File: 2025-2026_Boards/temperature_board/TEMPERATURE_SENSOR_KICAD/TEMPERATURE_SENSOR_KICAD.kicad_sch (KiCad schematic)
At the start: 39 parts, among them U1 STM32G431CBT6, U2 TMP235A4DBZR, U3 AMS1117-3.3, U4 TPS54240DGQ

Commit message: added voltage regulators. wired lcd pinout. added fan pinouts. added 2nd buck converter.
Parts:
- added C24, C25: 22u, Capacitor_SMD:C_0805_2012Metric, symbol Device:C
- added Cboot, Css, Css1: 33n, symbol Device:C
- added Cboot1, Cinx, Cinx1: 100n, symbol Device:C
- added Cin, Cin1: 10u, symbol Device:C
- added Cout, Cout1: 47u, symbol Device:C
- added D10, D11, D12, D13, D14, D15, D16, D17, D18, D19, D20, D21, D22, D23, D24, D25, D26, D27, D28, D29, D3, D30, D31, D32, D33, D34, D4, D5, D6, D7, D8, D9: 1N4148WT, Diode_SMD:D_SOD-523, symbol Diode:1N4148WT
- added D35: LED, Capacitor_SMD:C_0201_0603Metric, symbol Device:LED
- added J1: LCD Connector Pinout, symbol Connector_Generic_MountingPin:Conn_01x12_MountingPin
- added J2, J3: Conn_01x03_Pin, symbol Connector:Conn_01x03_Pin
- added L2: 10u, symbol Device:L
- added L3: 22u, symbol Device:L
- added R9: 1k5, Resistor_SMD:R_0402_1005Metric, symbol Device:R
- added RR1: 130, Resistor_SMD:R_0402_1005Metric, symbol Device:R
- added RR2: 100, Resistor_SMD:R_0402_1005Metric, symbol Device:R
- added Rfbb, Rfbb1: 10k, symbol Device:R
- added Rfbt: 52.3k, symbol Device:R
- added Rfbt1: 140k, symbol Device:R
- added U5, U6: TPS62932DRLR, SOT8_DRL_TEX, symbol 2025-10-19_16-52-39:TPS62932DRLR
- added U8: AMS1117, Package_TO_SOT_SMD:SOT-223-3_TabPin2, symbol Regulator_Linear:AMS1117
- L1: value L -> 10u
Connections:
- net +28V: now also C24.2, C25.1, C25.2, Cin.2, Cin1.2, Cinx.2, Cinx1.2, Cout.2, Cout1.2, Css.2, Css1.2, D35.2 (A), J2.2 (Pin_2), J3.2 (Pin_2), R9.2, RR1.1, RR2.2, Rfbb.2, Rfbb1.2, U5.4 (GND), U6.4 (GND), U8.2 (VO)
- net PWR_LED_K: now also D35.1 (K), R9.1
- net VBUS renamed +5V
- net +5V: now also C24.1, J3.1 (Pin_1), U8.3 (VI)
- new net: D12.1 (K), D25.1 (K), D28.1 (K), D4.1 (K), J1.7 (Pin_7)
- new net: D11.2 (A), D12.2 (A), D13.2 (A), D14.2 (A), D15.2 (A), D16.2 (A), D17.2 (A), D18.2 (A), J1.9 (Pin_9)
- new net: Cboot1.1, U6.6 (BST)
- new net: Cboot1.2, L3.1, U6.5 (SW)
- new net: D13.1 (K), D24.1 (K), D29.1 (K), D5.1 (K), J1.4 (Pin_4)
- new net: D27.2 (A), D28.2 (A), D29.2 (A), D30.2 (A), D31.2 (A), D32.2 (A), D33.2 (A), D34.2 (A), J1.6 (Pin_6)
- new net: D15.1 (K), D22.1 (K), D31.1 (K), D7.1 (K), J1.1 (Pin_1)
- new net: D19.2 (A), D20.2 (A), D21.2 (A), D22.2 (A), D23.2 (A), D24.2 (A), D25.2 (A), D26.2 (A), J1.8 (Pin_8)
- new net: D14.1 (K), D23.1 (K), D30.1 (K), D6.1 (K), J1.2 (Pin_2)
- new net: D10.1 (K), D18.1 (K), D19.1 (K), D34.1 (K), J1.3 (Pin_3)
- new net: D10.2 (A), D3.2 (A), D4.2 (A), D5.2 (A), D6.2 (A), D7.2 (A), D8.2 (A), D9.2 (A), J1.12 (Pin_12)
- new net: D11.1 (K), D26.1 (K), D27.1 (K), D3.1 (K), J1.11 (Pin_11)
- new net: Rfbb1.1, Rfbt1.2, U6.8 (FB)
- new net: D16.1 (K), D21.1 (K), D32.1 (K), D8.1 (K), J1.10 (Pin_10)
- new net: D17.1 (K), D20.1 (K), D33.1 (K), D9.1 (K), J1.5 (Pin_5)
- new net: Rfbb.1, Rfbt.2, U5.8 (FB)
- new net: Css1.1, U6.7 (SS)
- new net: RR1.2, RR2.1, U8.1 (ADJ)
- new net: Cboot.1, U5.6 (BST)
- new net: Cboot.2, L2.1, U5.5 (SW)
- new net: Css.1, U5.7 (SS)
- new net +12V: J2.1 (Pin_1)
- new net 12V: Cout1.1, L3.2, Rfbt1.1
- new net 28V: Cin.1, Cin1.1, Cinx.1, Cinx1.1, U5.3 (VIN), U6.3 (VIN)
- new net 5V: Cout.1, L2.2, Rfbt.1
- no-connect marks 0 -> 4
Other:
- note added: "BUCK CONVERTER (28V TO 12V, 2A)"
- note added: "BUCK CONVERTER (28V TO 5V, 2A)"
- note added: "CAMERA FAN PINOUT"
- note added: "ECORE FAN PINOUT"
- note added: "FAN PINOUTS"
- note added: "ON/OFF SIGNAL"
- note added: "STM32 / TMP23X VOLTAGE REGULATOR, 5V TO 3.3V"
- note removed: "FAN SYSTEMS AND POWER SUPPLY"
- note removed: "LCD AND POWER SUPPLY"
- note removed: "STM32 / TMP23X VOLTAGE REGULATOR"
- moved on the sheet: C1, C10, C11, C12, C13, C14, C15, C16, C17, C18, C19, C2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

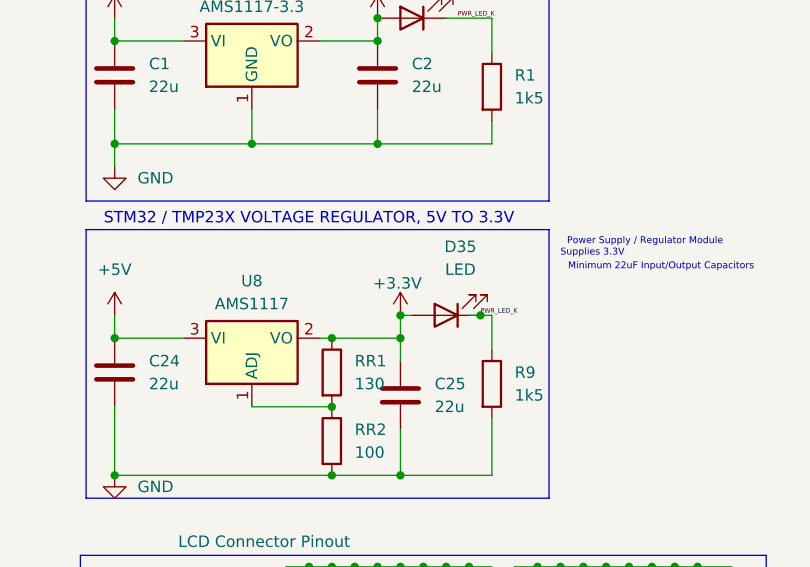
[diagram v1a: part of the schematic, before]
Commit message: 3.3->2.2V
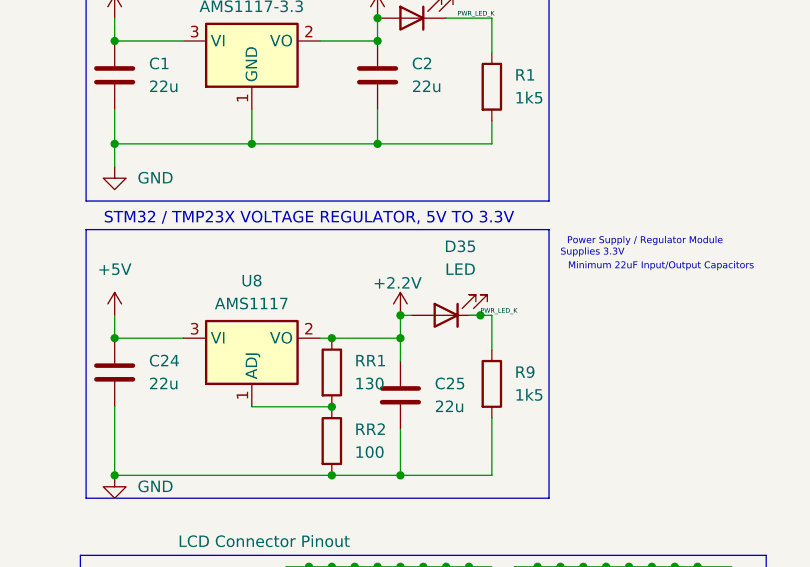
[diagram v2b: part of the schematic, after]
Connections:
- net +28V: no longer C25.1, D35.2 (A), RR1.1, U8.2 (VO)
- new net +2.2V: C25.1, D35.2 (A), RR1.1, U8.2 (VO)
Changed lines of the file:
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@@
 			)
 		)
-		(property "Value" "+3.3V"
+		(property "Value" "+2.2V"
 			(at 45.212 106.934 0)
 			(effects

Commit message: connected LCD pins to GPIO. Replicated ECORE fans and connectd to GPIO
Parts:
- removed J2: Conn_01x03_Pin, symbol Connector:Conn_01x03_Pin
- added J10, J11, J4, J5, J6, J7, J8, J9: Conn_01x03_Pin, symbol Connector:Conn_01x03_Pin
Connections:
- net +12V: now also J10.1 (Pin_1), J11.1 (Pin_1), J4.1 (Pin_1), J5.1 (Pin_1), J6.1 (Pin_1), J7.1 (Pin_1), J8.1 (Pin_1), J9.1 (Pin_1)
- net +28V: now also C14.1, J10.2 (Pin_2), J11.2 (Pin_2), J4.2 (Pin_2), J5.2 (Pin_2), J6.2 (Pin_2), J7.2 (Pin_2), J8.2 (Pin_2), J9.2 (Pin_2); no longer C14.2
- net at D12.1 (K), D25.1 (K), D28.1 (K)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: now also U1.17 (PB1)
- net at D11.2 (A), D12.2 (A), D13.2 (A)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: now also U1.5 (PF0)
- net at D13.1 (K), D24.1 (K), D29.1 (K)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: now also U1.41 (PB4)
- net at D27.2 (A), D28.2 (A), D29.2 (A)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: now also U1.28 (PB14)
- net at D15.1 (K), D22.1 (K), D31.1 (K)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: now also U1.44 (PB7)
- net at D19.2 (A), D20.2 (A), D21.2 (A)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: now also U1.29 (PB15)
- net at D14.1 (K), D23.1 (K), D30.1 (K)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: now also U1.43 (PB6)
- net at U1.11 (PA3): now also C14.2, R2.1
- net at U1.3 (PC14): now also D11.1 (K), D26.1 (K), D27.1 (K), D3.1 (K), J1.11 (Pin_11)
- net at U1.31 (PA9): now also J10.3 (Pin_3), J11.3 (Pin_3), J4.3 (Pin_3), J5.3 (Pin_3), J6.3 (Pin_3), J7.3 (Pin_3), J8.3 (Pin_3), J9.3 (Pin_3)
- net at U1.4 (PC15): now also D16.1 (K), D21.1 (K), D32.1 (K), D8.1 (K), J1.10 (Pin_10)
- net at U1.40 (PB3): now also D17.1 (K), D20.1 (K), D33.1 (K), D9.1 (K), J1.5 (Pin_5)
- net at U1.42 (PB5): now also D10.1 (K), D18.1 (K), D19.1 (K), D34.1 (K), J1.3 (Pin_3)
- net at U1.7 (PG10): now also D10.2 (A), D3.2 (A), D4.2 (A), D5.2 (A), D6.2 (A), D7.2 (A), D8.2 (A), D9.2 (A), J1.12 (Pin_12)
- now unconnected: U1.30 (PA8)
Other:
- note added: "STM32 / TMP23X VOLTAGE REGULATOR, 5V TO 2.2V"
- note removed: "FAN PINOUTS"
- moved on the sheet: C1, C10, C11, C12, C13, C14, C2, C24, C25, C3, C4, C5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

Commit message: Fixed fan pins in schematic. Started PCB layout. Wiring LDOs and buck converters.
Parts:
- removed C15, C16: 2.2u, Capacitor_SMD:C_0201_0603Metric, symbol Device:C
- removed C17: 0.01u, Capacitor_SMD:C_0201_0603Metric, symbol Device:C
- removed C18: C, symbol Device:C
- removed C19, C20, C23: 47u, symbol Device:C
- removed C21: 3300pf, Capacitor_SMD:C_0201_0603Metric, symbol Device:C
- removed C22: 15pf, Capacitor_SMD:C_0201_0603Metric, symbol Device:C
- removed D2: B360, Diode_SMD:D_SMC, symbol Diode:B360
- removed J10, J11, J3, J4, J5, J6, J7, J8, J9: Conn_01x03_Pin, symbol Connector:Conn_01x03_Pin
- removed L1: 10u, symbol Device:L
- removed R3: 124k, symbol Device:R
- removed R4: 30.1k, symbol Device:R
- removed R5: 412k, symbol Device:R
- removed R6: 37.4k, symbol Device:R
- removed R7: 10.0k, symbol Device:R
- removed R8: 45.3k, symbol Device:R
- removed U4: TPS54240DGQ, Package_SO:HVSSOP-10-1EP_3x3mm_P0.5mm_EP1.57x1.88mm_ThermalVias, symbol Converter_DCDC:TPS54240DGQ
- C14, Cboot1: footprint (none) -> Capacitor_SMD:C_0402_1005Metric
- Cboot2: renamed from Cboot; footprint (none) -> Capacitor_SMD:C_0201_0603Metric
- Cin1, Cout1: footprint (none) -> Capacitor_SMD:C_1210_3225Metric
- Cin2: renamed from Cin; footprint (none) -> Capacitor_SMD:C_1210_3225Metric
- Cinx1: footprint (none) -> Capacitor_SMD:C_0603_1608Metric
- Cinx2: renamed from Cinx; footprint (none) -> Capacitor_SMD:C_0603_1608Metric
- Cout2: renamed from Cout; footprint (none) -> Capacitor_SMD:C_1210_3225Metric
- Css1: footprint (none) -> Capacitor_SMD:C_01005_0402Metric
- Css2: renamed from Css; footprint (none) -> Capacitor_SMD:C_01005_0402Metric
- J1: footprint (none) -> Connector_FFC-FPC:Amphenol_F32Q-1A7x1-11012_1x12-1MP_P0.5mm_Horizontal
- L2: footprint (none) -> Inductor_SMD:L_Bourns_SRR1208_12.7x12.7mm
- L3: footprint (none) -> Inductor_THT:L_Radial_D13.5mm_P7.00mm_Fastron_09HCP
- R2: value 10R -> 10k; footprint (none) -> Resistor_SMD:R_0402_1005Metric
- Rfbb1: footprint (none) -> Resistor_SMD:R_0402_1005Metric
- Rfbb2: renamed from Rfbb; footprint (none) -> Resistor_SMD:R_0402_1005Metric
- Rfbt1: footprint (none) -> Resistor_SMD:R_0201_0603Metric
- Rfbt2: renamed from Rfbt; footprint (none) -> Resistor_SMD:R_0603_1608Metric
- U2: footprint DBZ0003A-IPC_A -> AdditionalFootprintLibrary:DBZ0003A-IPC_A
- U5, U6: footprint SOT8_DRL_TEX -> AdditionalFootprintLibrary:SOT8_DRL_TEX-M
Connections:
- net PWR_LED_K: no longer D35.1 (K), R9.1
- net +28V renamed GND
- net GND: no longer C11.1, C12.1, C13.1, C2.1, C3.1, C4.1, C5.1, C6.1, C7.1, D1.2 (A), U1.1 (VBAT), U1.24 (VDD), U1.36 (VDD), U1.48 (VDD), U2.1 (VDD), U3.2 (VO)
- new net: D35.1 (K), R9.1
- new net +3.3V: C11.1, C12.1, C13.1, C2.1, C3.1, C4.1, C5.1, C6.1, C7.1, D1.2 (A), U1.1 (VBAT), U1.24 (VDD), U1.36 (VDD), U1.48 (VDD), U2.1 (VDD), U3.2 (VO)
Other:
- added sheet Fan_Pins (FAN_PINS.kicad_sch)
- note added: "Supplies 2.2V"
- note removed: "BUCK CONVERTER (Early Draft, subject to change)"
- note removed: "CAMERA FAN PINOUT"
- note removed: "ECORE FAN PINOUT"
- note removed: "ON/OFF SIGNAL"
- moved on the sheet: C1, C2, C24, C25, D1, D35, R1, R9, RR1, RR2, U3, U8

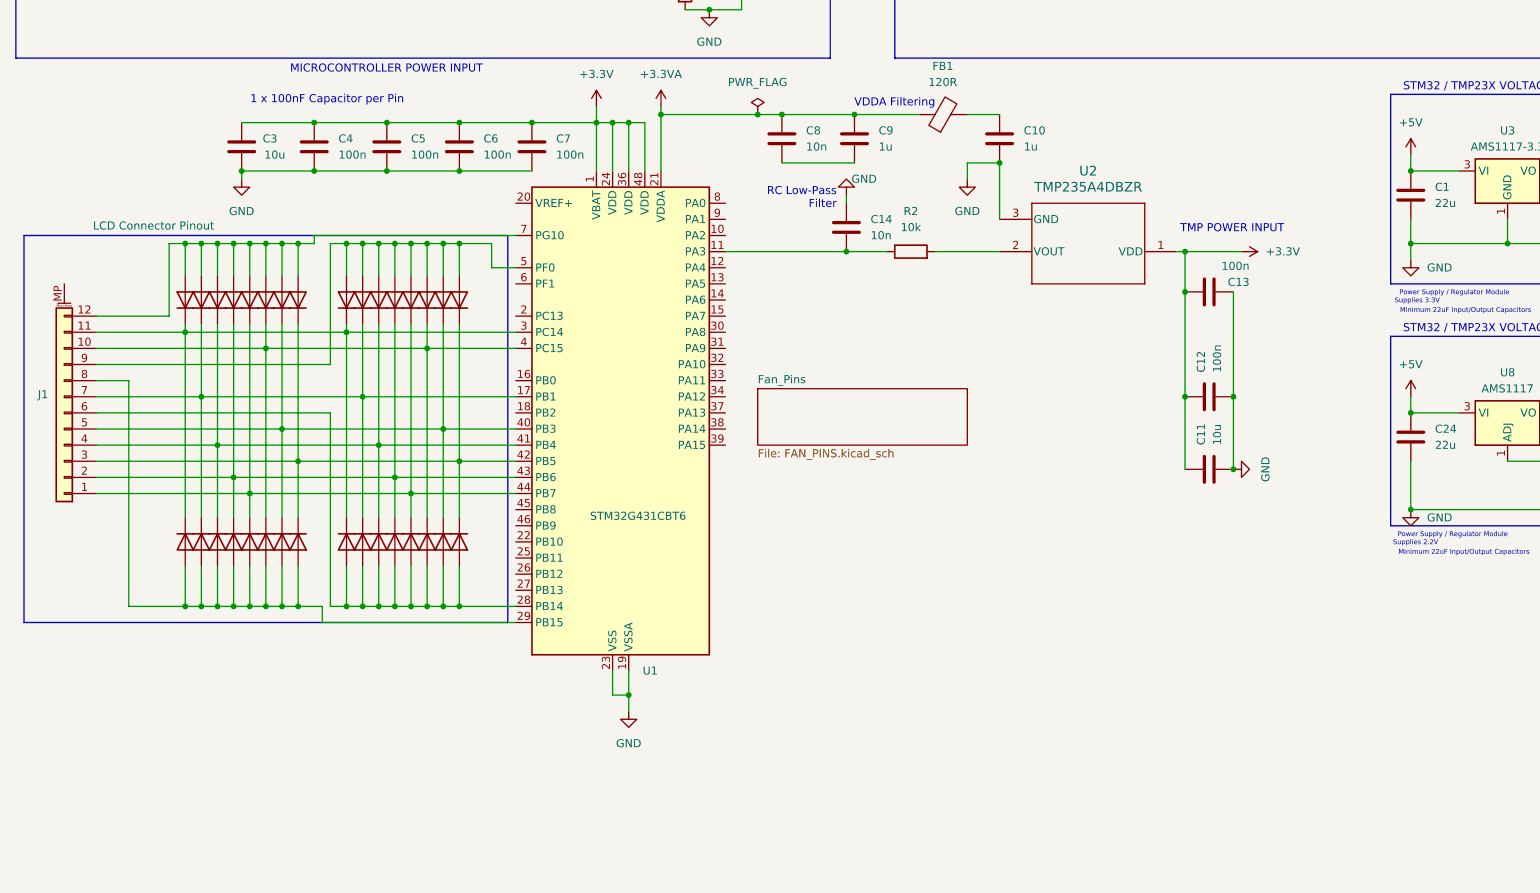
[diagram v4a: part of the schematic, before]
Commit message: Almost finished wiring. Just need to adjust widths and check configuration before finalizing design
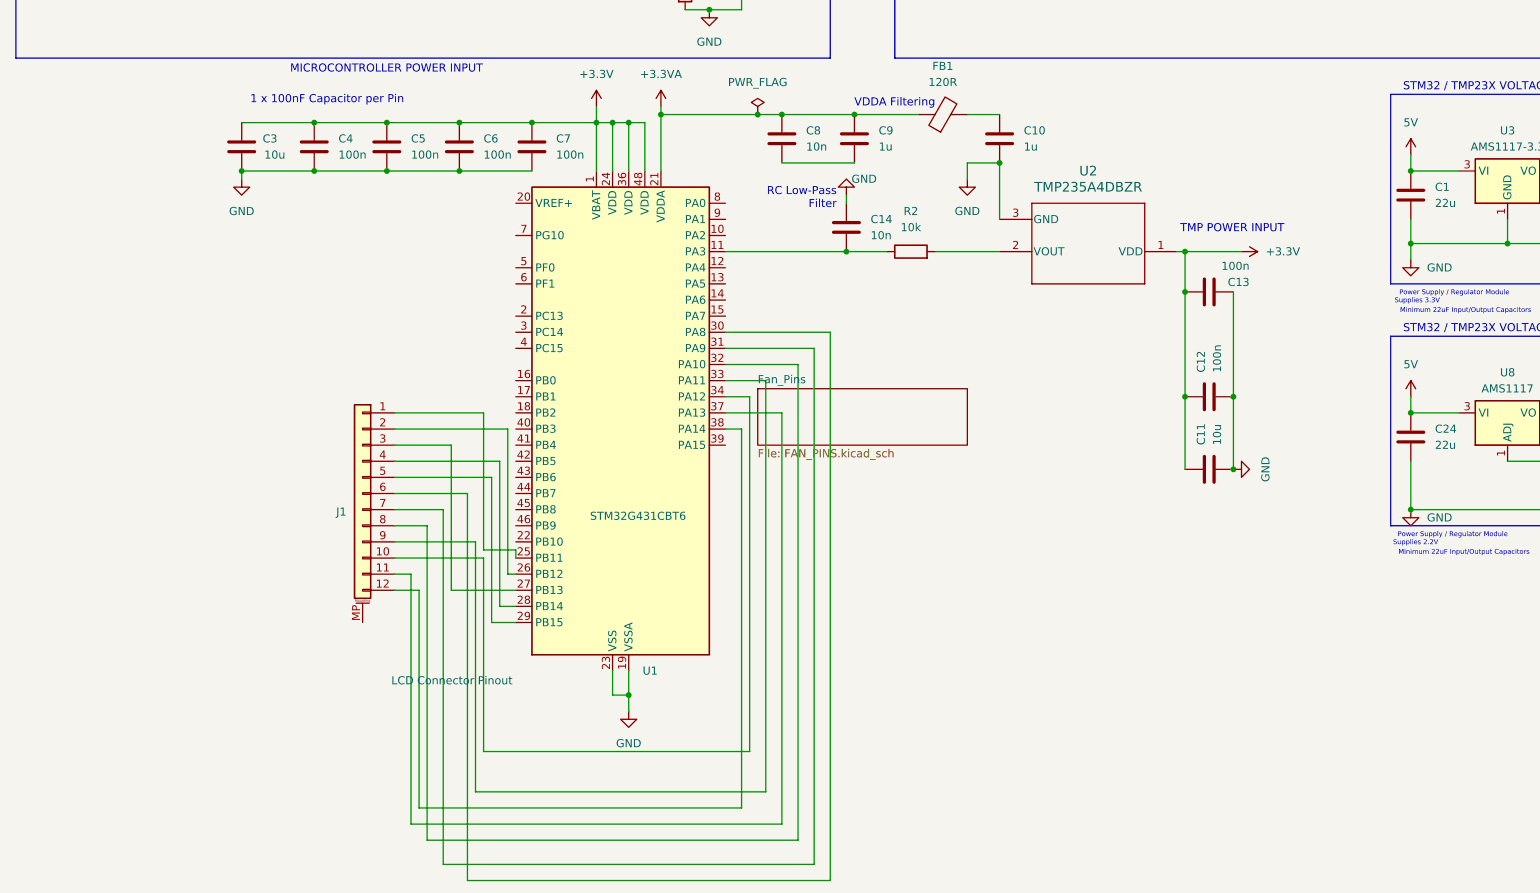
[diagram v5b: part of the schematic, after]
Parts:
- removed D10, D11, D12, D13, D14, D15, D16, D17, D18, D19, D20, D21, D22, D23, D24, D25, D26, D27, D28, D29, D3, D30, D31, D32, D33, D34, D4, D5, D6, D7, D8, D9: 1N4148WT, Diode_SMD:D_SOD-523, symbol Diode:1N4148WT
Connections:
- net +5V is gone; now on net 5V: C1.1, C24.1, U3.3 (VI), U8.3 (VI)
- net at U1.17 (PB1): no longer J1.7 (Pin_7)
- net at J1.9 (Pin_9): now also U1.33 (PA11); no longer U1.5 (PF0)
- net at J1.4 (Pin_4): now also U1.28 (PB14); no longer U1.41 (PB4)
- net at J1.6 (Pin_6): now also U1.30 (PA8); no longer U1.28 (PB14)
- net at J1.1 (Pin_1): now also U1.25 (PB11); no longer U1.44 (PB7)
- net at U1.29 (PB15): now also J1.5 (Pin_5); no longer J1.8 (Pin_8)
- net at J1.2 (Pin_2): now also U1.26 (PB12); no longer U1.43 (PB6)
- net at U1.27 (PB13): now also J1.3 (Pin_3)
- net at U1.3 (PC14): no longer J1.11 (Pin_11)
- net at U1.31 (PA9): now also J1.7 (Pin_7)
- net at U1.32 (PA10): now also J1.8 (Pin_8)
- net at U1.34 (PA12): now also J1.10 (Pin_10)
- net at U1.37 (PA13): now also J1.11 (Pin_11)
- net at U1.38 (PA14): now also J1.12 (Pin_12)
- net at U1.4 (PC15): no longer J1.10 (Pin_10)
- net at U1.40 (PB3): no longer J1.5 (Pin_5)
- net at U1.42 (PB5): no longer J1.3 (Pin_3)
- net at U1.7 (PG10): no longer J1.12 (Pin_12)
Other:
- moved on the sheet: J1

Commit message: Finishing up
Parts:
- added TP1, TP2, TP3, TP4, TP5, TP6: TestPoint, symbol Connector:TestPoint
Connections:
- net +2.2V: now also U1.13 (PA5)
- net +3.3V: now also TP1.1
- net 12V: now also TP5.1
- net 5V: now also TP4.1
- new net 2.2V: TP3.1

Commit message: minor updates
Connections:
- net at U1.14 (PA6): now also J1.9 (Pin_9)
- net at U1.15 (PA7): now also J1.10 (Pin_10)
- net FDCAN_RX: now reaches U1.33 (PA11)
- net FDCAN_RX: no longer J1.9 (Pin_9)
- net FDCAN_TX: now reaches U1.34 (PA12)
- net FDCAN_TX: no longer J1.10 (Pin_10)
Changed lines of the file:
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@@
-	(wire
-		(pts
-			(xy 128.27 118.11) (xy 124.46 118.11)
-		)
-		(stroke
-			(width 0)
-			(type default)
-		)
-	)
 	(wire
 		(pts
@@
 	(wire
 		(pts
-			(xy 130.81 115.57) (xy 124.46 115.57)
-		)
-		(stroke
-			(width 0)
-			(type default)
-		)
-	)
-	(wire
-		(pts
 			(xy 90.17 123.19) (xy 90.17 146.05)
 		)
@@
 	(wire
 		(pts
+			(xy 128.27 105.41) (xy 124.46 105.41)
+		)
+		(stroke
+			(width 0)
+			(type default)
+		)
+	)
+	(wire
+		(pts
 			(xy 86.36 120.65) (xy 86.36 142.24)
 		)
@@
 	(wire
 		(pts
-			(xy 130.81 180.34) (xy 130.81 115.57)
+			(xy 130.81 102.87) (xy 130.81 180.34)
 		)
 		(stroke
@@
 	(wire
 		(pts
-			(xy 128.27 173.99) (xy 128.27 118.11)
+			(xy 128.27 105.41) (xy 128.27 173.99)
 		)
 		(stroke
@@
 		(pts
 			(xy 106.68 74.93) (xy 106.68 82.55)
+		)
+		(stroke
+			(width 0)
+			(type default)
+		)
+	)
+	(wire
+		(pts
+			(xy 130.81 102.87) (xy 124.46 102.87)
 		)
 		(stroke
@@
 		)
 	)
+	(global_label "FDCAN_TX"
+		(shape input)
+		(at 124.46 118.11 0)
+		(fields_autoplaced yes)
+		(effects
+			(font
+				(size 1.27 1.27)
+			)
+			(justify left)
+		)
+		(property "Intersheetrefs" "${INTERSHEET_REFS}"
+			(at 136.6376 118.11 0)
+			(effects
+				(font
+					(size 1.27 1.27)
+				)
+				(justify left)
+				(hide yes)
+			)
+		)
+	)
+	(global_label "FDCAN_RX"
+		(shape input)
+		(at 124.46 115.57 0)
+		(fields_autoplaced yes)
+		(effects
+			(font
+				(size 1.27 1.27)
+			)
+			(justify left)
+		)
+		(property "Intersheetrefs" "${INTERSHEET_REFS}"
+			(at 136.94 115.57 0)
+			(effects
+				(font
+					(size 1.27 1.27)
+				)
+				(justify left)
+				(hide yes)
+			)
+		)
+	)

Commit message: finishing the board. debuggign,ectc
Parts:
- removed TP5, TP6: TestPoint, symbol Connector:TestPoint
- added H1, H2, H3, H4: MountingHole, MountingHole:MountingHole_4.3mm_M4, symbol Mechanical:MountingHole
- TP1, TP2, TP3, TP4: footprint (none) -> Connector_Pin:Pin_D1.3mm_L10.0mm_W3.5mm_Flat
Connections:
- net 2.2V is gone; now on net 5V: TP3.1
- net +2.2V: now also TP4.1
- net 12V: now also TP2.1
- net 5V: no longer TP4.1
